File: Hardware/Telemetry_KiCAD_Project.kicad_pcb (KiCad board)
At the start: 4 copper layers, 80 x 87.3 mm, 68 parts, among them J1 TX SPI Debug, J2 RX SPI Debug, J3 50Ω SMA Connector, J4 10118192-0001LF, J5 DB37_Male_MountingHoles, U1 STM32L562VET, U2 Si4463, U3 Si4463, U4 ADL5521, U5 RSD-897.500-942.500-1612-TR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

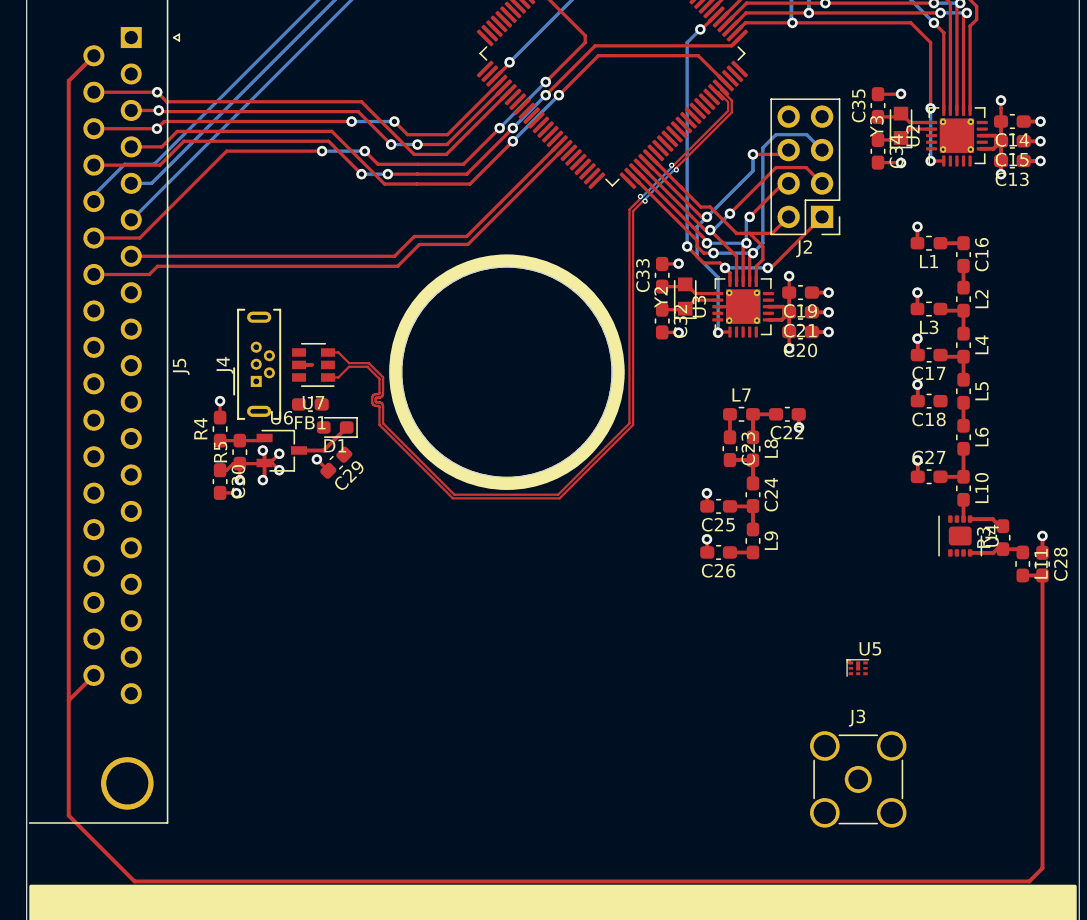
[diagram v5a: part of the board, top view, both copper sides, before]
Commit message: Routed RF traces
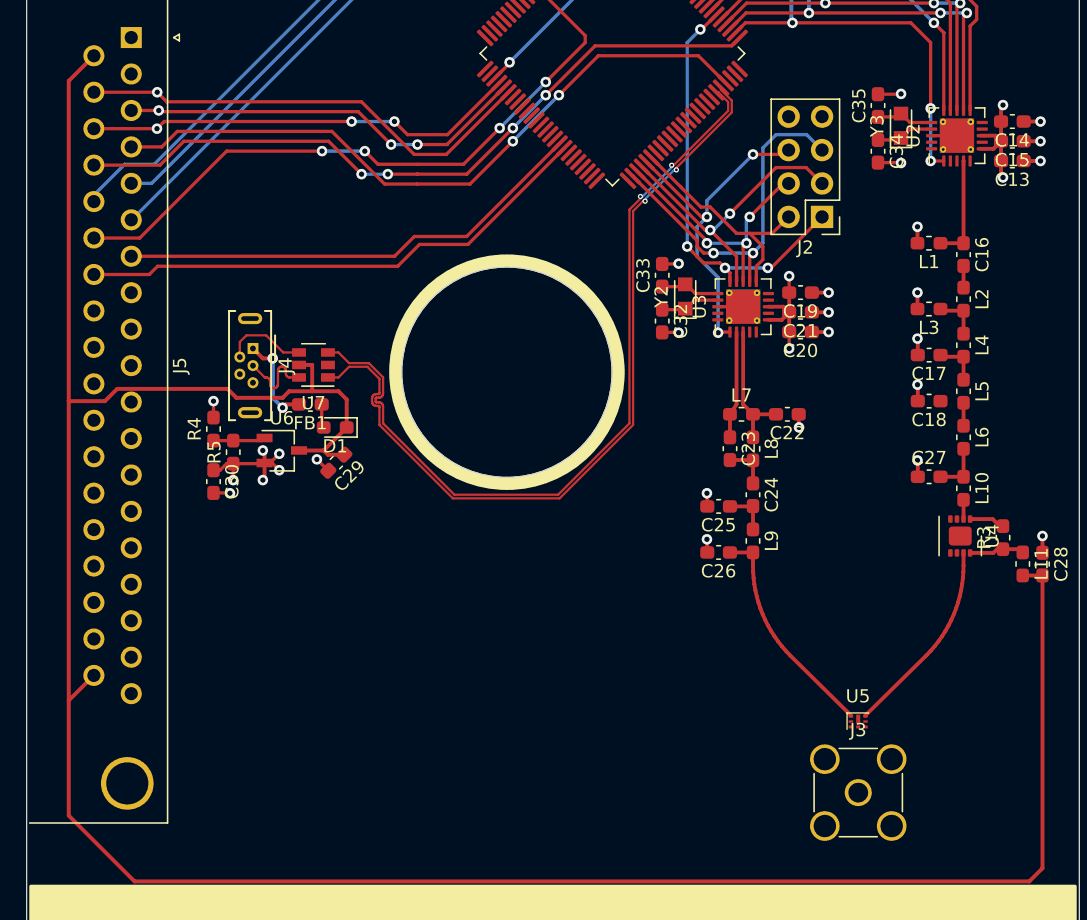
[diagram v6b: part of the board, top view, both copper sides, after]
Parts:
- moved U5 4.05 mm to (169.2, 125.0)
- moved J4 2.51 mm to (124.0, 97.2), turned to 270 degrees
- moved J3 1.00 mm to (170.0, 131.0)
- moved C30 0.50 mm to (121.0, 107.4)
- moved R4 0.50 mm to (121.0, 103.4)
- moved R5 0.50 mm to (122.5, 105.1)
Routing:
- net +5V: track 166.8 -> 194.9 mm
- net /ADL_Amplifier/RF_Out: track 0.00 -> 15.1 mm
- net /RX_Si4463/RF_Out: track 1.89 -> 16.8 mm
- net Net-(FB1-Pad2): track 0.00 -> 7.22 mm, vias 0 -> 2
- net Net-(C22-Pad2): track 3.50 -> 10.1 mm
- net Net-(C23-Pad1): track 2.35 -> 8.75 mm
- net /USB Connector and ESD/USB_CONN_D+: track 0.00 -> 6.40 mm
- net /USB Connector and ESD/USB_CONN_D-: track 0.00 -> 6.40 mm
- net Net-(C16-Pad1): track 1.63 -> 7.88 mm
- net GND: track 25.2 -> 27.1 mm, vias 19 -> 21
- net Net-(D1-Pad2): track 0.00 -> 1.81 mm
- net +3V3: track 29.0 -> 29.5 mm, vias 9 -> 10
- net (no net): vias 3 -> 0

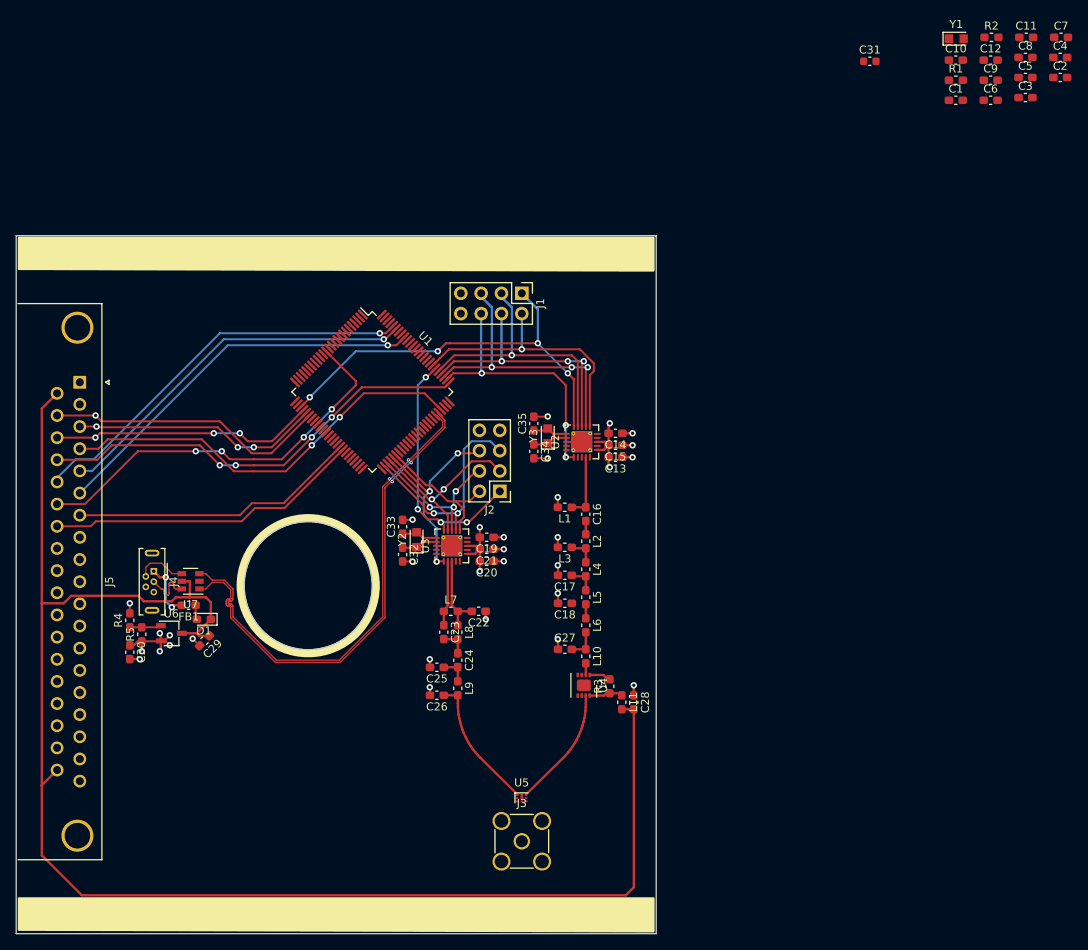
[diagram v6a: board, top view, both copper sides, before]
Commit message: Added via fences to RF traces
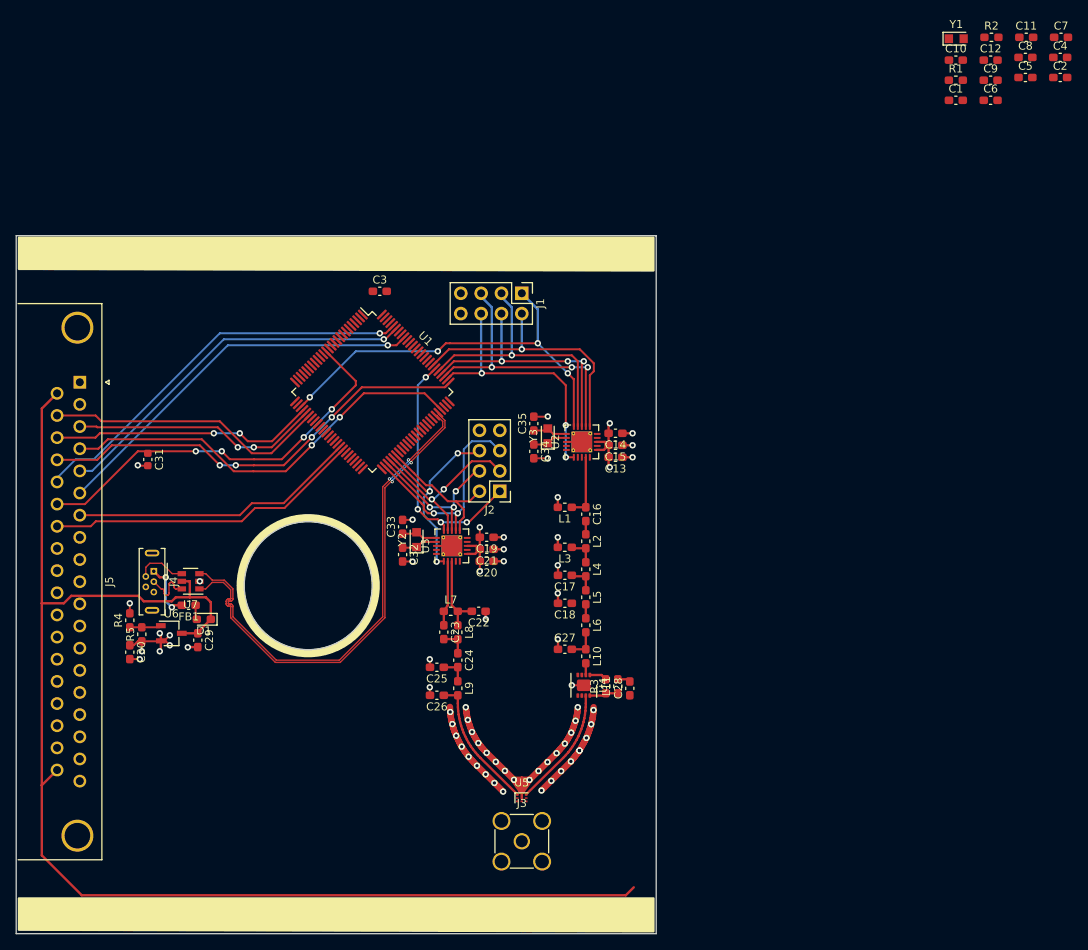
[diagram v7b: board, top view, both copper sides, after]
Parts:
- moved C31 103.1 mm to (123.2, 83.3), turned to 270 degrees
- moved C3 84.3 mm to (152.2, 62.2)
- moved L11 2.06 mm to (182.0, 111.6), turned to 90 degrees
- moved C28 1.82 mm to (183.5, 111.9), turned to 90 degrees
- moved C29 0.84 mm to (129.5, 105.9), turned to 270 degrees
- moved R3 0.50 mm to (180.5, 111.6)
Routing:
- net GND: track 27.1 -> 83.4 mm, vias 21 -> 57
- net +5V: track 194.9 -> 171.1 mm
- net /MCU_L562VE/SPI1_SCK: vias 3 -> 2
- net /MCU_L562VE/SPI1_MOSI: vias 1 -> 0
- net /MCU_L562VE/SPI1_MISO: vias 3 -> 2

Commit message: Placed decoupling capacitors for MCU
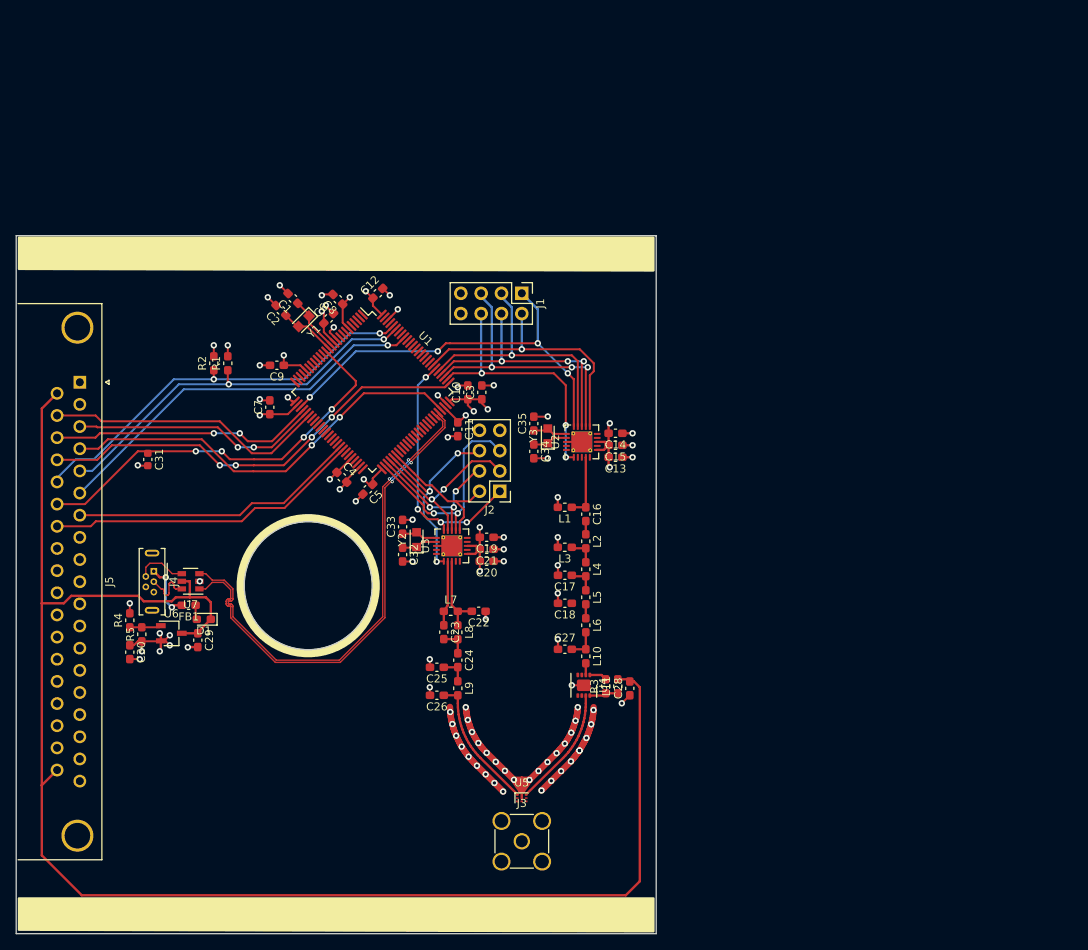
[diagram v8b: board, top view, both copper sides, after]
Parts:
- moved C7 109.2 mm to (138.5, 76.8), turned to 90 degrees
- moved R2 105.4 mm to (131.5, 71.2), turned to 90 degrees
- moved C4 104.0 mm to (147.5, 85.5), turned to 315 degrees
- moved C2 101.7 mm to (139.9, 64.6), turned to 135 degrees
- moved R1 97.6 mm to (133.2, 71.2), turned to 90 degrees
- moved C5 97.0 mm to (150.8, 87.0), turned to 225 degrees
- moved C9 96.1 mm to (139.4, 71.5), turned to 180 degrees
- moved C8 91.1 mm to (147.0, 63.2), turned to 135 degrees
- moved Y1 88.9 mm to (142.8, 66.0), turned to 225 degrees
- moved C6 87.1 mm to (145.9, 65.6), turned to 45 degrees
- moved C1 86.5 mm to (141.4, 63.1), turned to 135 degrees
- moved C11 86.3 mm to (162.0, 79.5), turned to 270 degrees
- moved C12 82.0 mm to (152.0, 62.5), turned to 45 degrees
- moved C10 73.8 mm to (163.2, 74.9), turned to 90 degrees
- moved C3 18.0 mm to (165.0, 74.9), turned to 90 degrees
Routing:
- net +3V3: track 29.5 -> 74.0 mm, vias 10 -> 22
- net GND: track 83.4 -> 113.1 mm, vias 57 -> 74
- net +5V: track 171.1 -> 198.0 mm
- net Net-(C2-Pad1): track 0.00 -> 7.30 mm
- net Net-(C1-Pad1): track 0.00 -> 7.06 mm
- net (no net): track 2.52 -> 0.00 mm
- net /37 Pin DSUB/Alert_scl: track 46.9 -> 48.7 mm, vias 1 -> 2
- net /37 Pin DSUB/Alert_sda: track 50.4 -> 51.5 mm, vias 1 -> 2
